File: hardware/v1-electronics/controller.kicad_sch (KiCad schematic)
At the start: 8 parts, among them J2 Conn_01x03, SW78 SW_Push, U1 MDBT50Q-1MV2

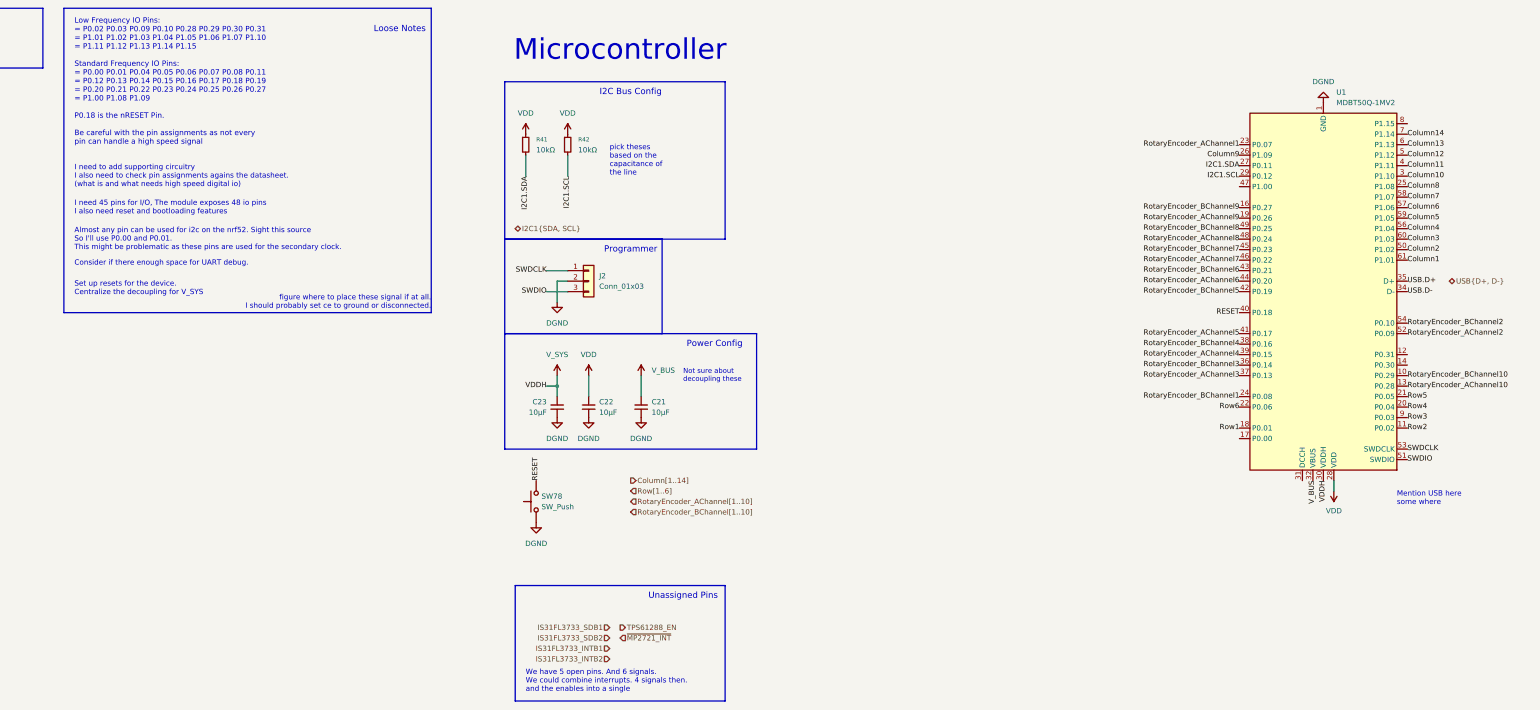
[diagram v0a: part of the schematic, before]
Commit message: refactor(v1 hardware): get references in order
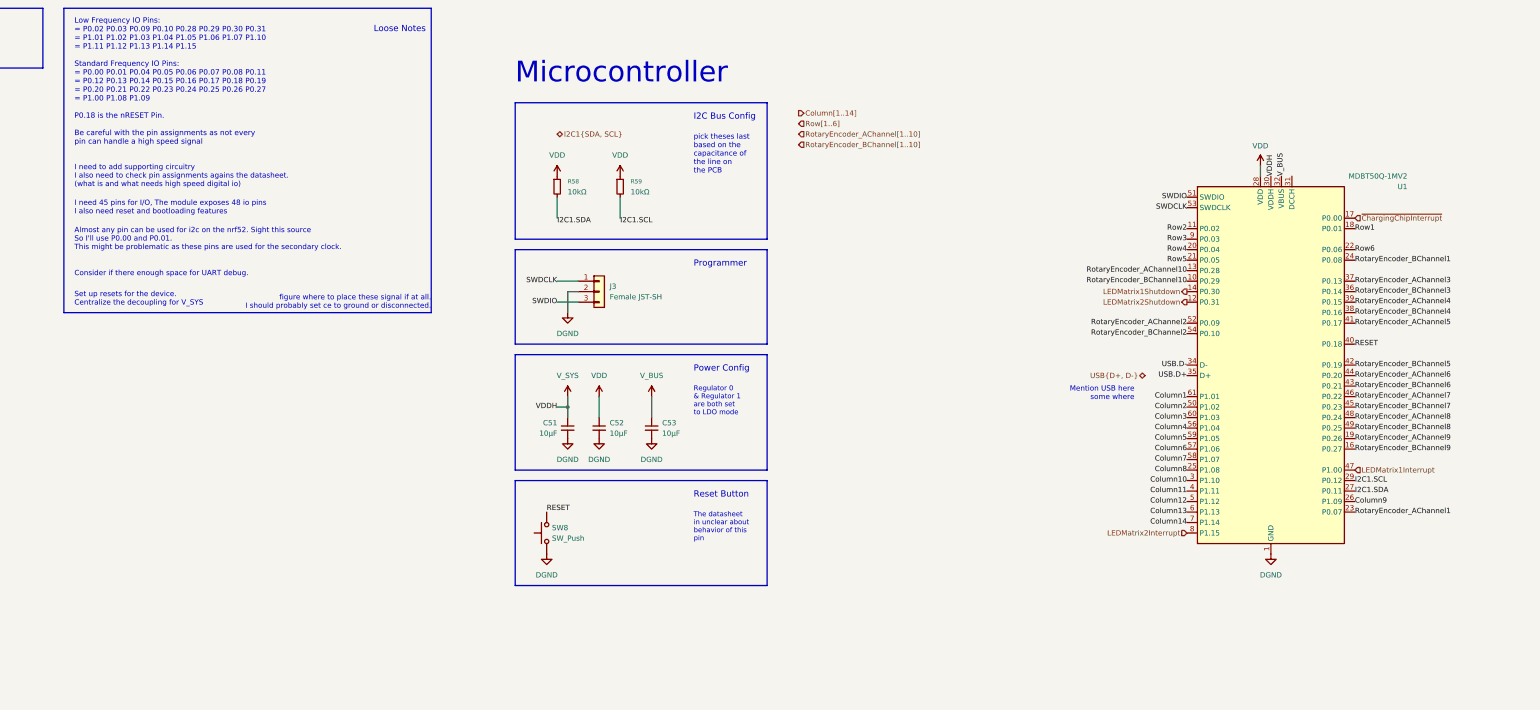
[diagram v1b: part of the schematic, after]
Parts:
- J3: renamed from J2; value Conn_01x03 -> Female JST-SH
- renumbered C23 to C51, C22 to C52, C21 to C53, R41 to R58, R42 to R59, SW78 to SW8
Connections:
- net LEDMatrix2Shutdown: now reaches U1.12 (P0.31)
- net LEDMatrix1Shutdown: now reaches U1.14 (P0.30)
- net ~{ChargingChipInterrupt}: now reaches U1.17 (P0.00)
- net LEDMatrix1Interrupt: now reaches U1.47 (P1.00)
- net LEDMatrix2Interrupt: now reaches U1.8 (P1.15)
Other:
- note added: "Regulator 0 & Regulator 1 are both set to LDO mode"
- note added: "Reset Button"
- note added: "The datasheet in unclear about behavior of this pin"
- note added: "pick theses last based on the capacitance of the line on the PCB"
- note removed: "Not sure about decoupling these"
- note removed: "Unassigned Pins"
- note removed: "We have 5 open pins. And 6 signals. We could combine interrupts. 4 signals then. and the enables into a single"
- note removed: "pick theses based on the capacitance of the line"
- moved on the sheet: C51, C52, C53, J3, R58, R59, SW8, U1
